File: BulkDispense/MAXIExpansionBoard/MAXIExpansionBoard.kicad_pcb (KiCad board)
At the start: 2 copper layers, 139.7 x 100 mm, 39 parts, among them J1 R0~R5, J10 FS2~FS4, J11 MV1~4, J12 WB/WL, J13 PS/PCV, J14 RV1&2, J15 RV3&4, J16 FS1, J17 FS3, J18 WB-MV1~4, J19 FS2, J2 BS1~4, J20 FS4, J21 BS1~4, J22 OS1~4, J23 WB-MV5~6, J24 LDS, J3 Screw_Terminal_01x02, J4 DigitalOUT 0~3, J5 DigitalOUT 4~7, J6 OS1~4, J7 AnalogIOs, J8 Fan PWR, J9 FS1

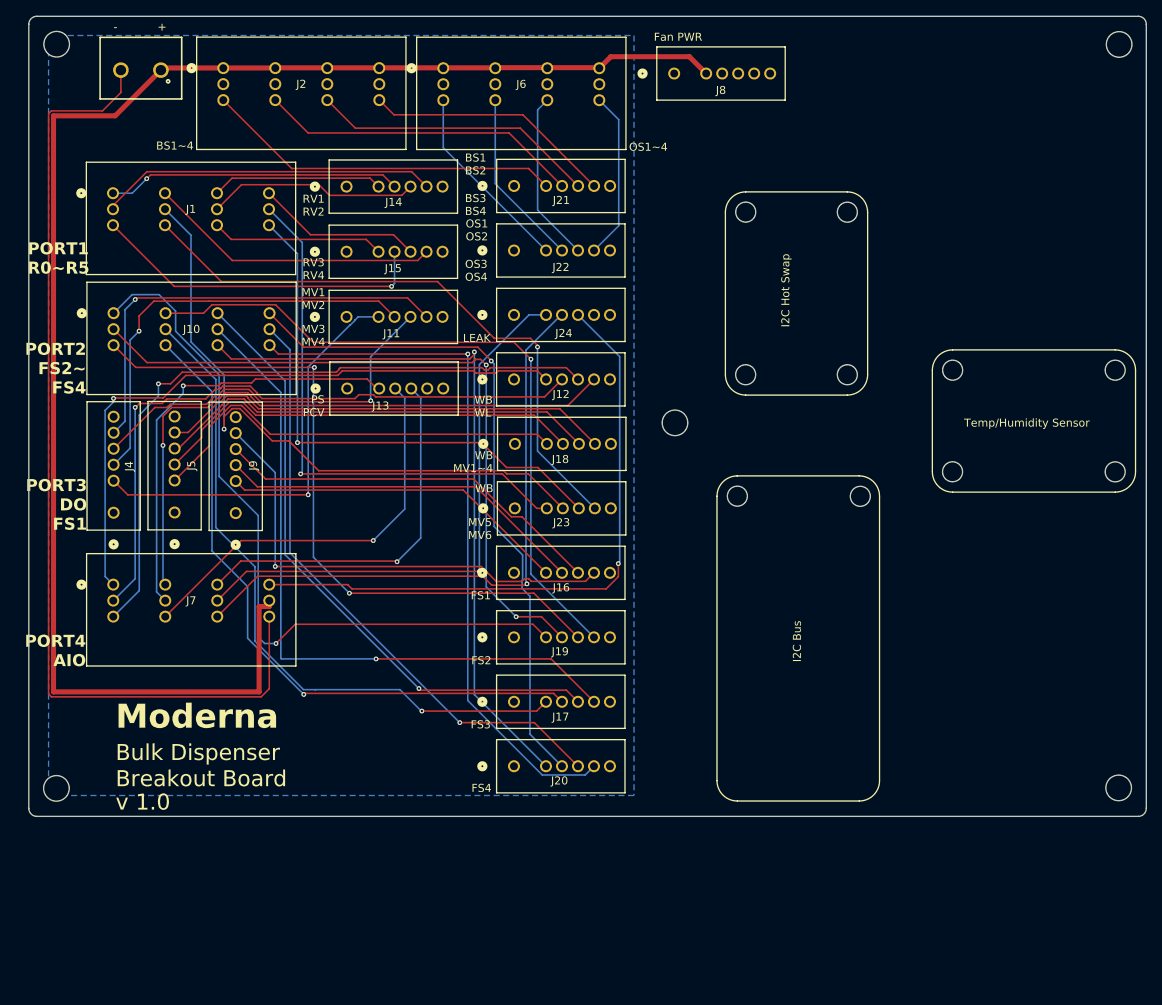
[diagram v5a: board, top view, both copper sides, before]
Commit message: Add PCB Revisions
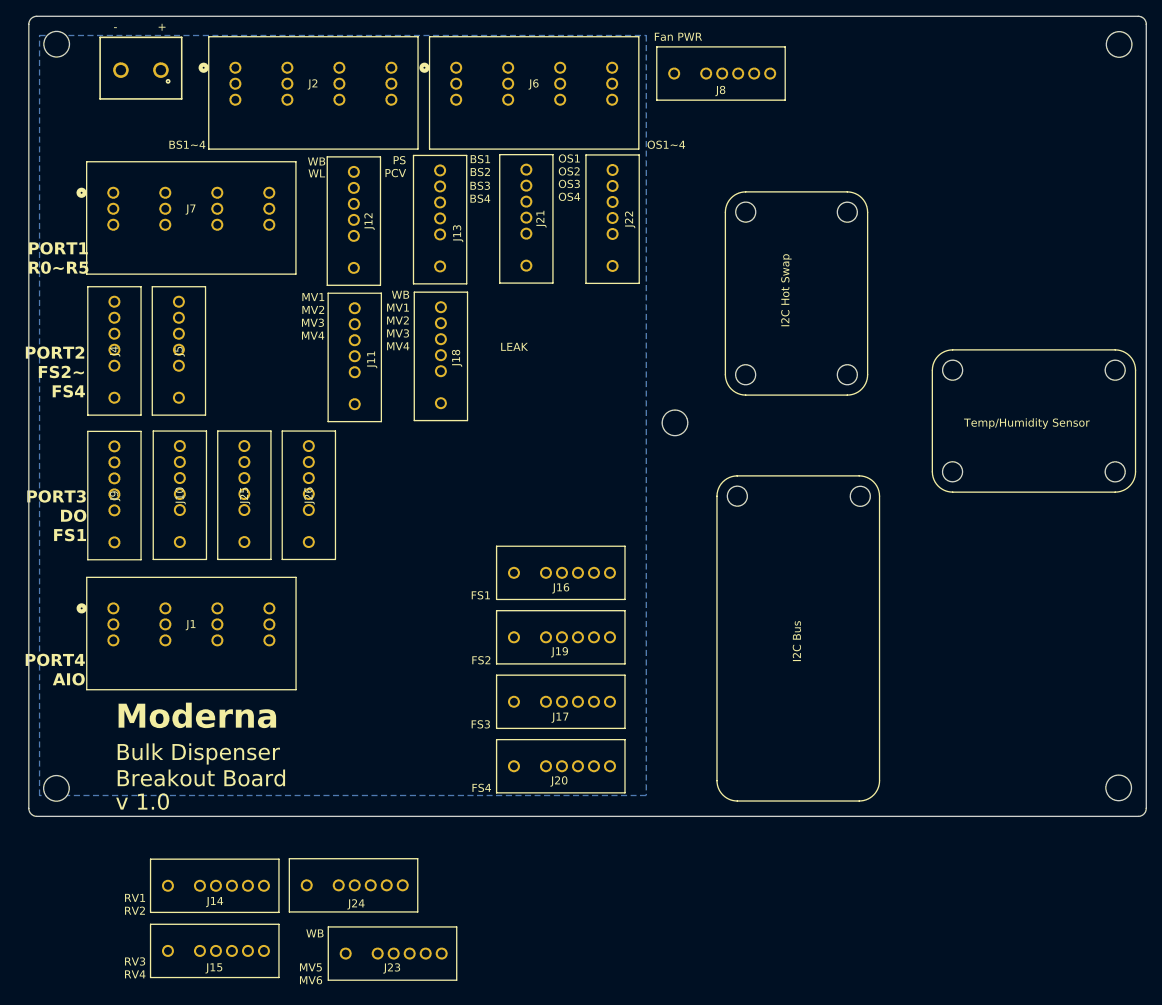
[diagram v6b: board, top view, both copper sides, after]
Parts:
- added J25: FS3, PartsLibrary:CONN_37204-62A3-004PL_3MM, F.Cu at (149.7, 102.1)
- added J26: FS4, PartsLibrary:CONN_37204-62A3-004PL_3MM, F.Cu at (157.8, 102.1)
- J1: value R0~R5 -> PWR
- J10: value FS2~FS4 -> FS2; footprint PartsLibrary:CONN_37212-62M3-003PL_3MM -> PartsLibrary:CONN_37204-62A3-004PL_3MM
- moved J15 90.2 mm to (144.2, 157.2)
- moved J14 90.2 mm to (144.2, 149.0)
- moved J24 75.9 mm to (161.5, 149.0)
- moved J23 59.5 mm to (166.4, 157.5)
- moved J1 51.9 mm to (133.3, 114.4)
- moved J7 49.0 mm to (133.3, 62.4)
- moved J12 30.0 mm to (163.4, 67.8), turned to 90 degrees
- moved J10 26.0 mm to (141.7, 102.1), turned to 90 degrees
- moved J13 20.7 mm to (174.2, 67.6), turned to 90 degrees
- moved J18 16.1 mm to (174.3, 84.7), turned to 90 degrees
- moved J9 15.6 mm to (133.5, 102.1)
- moved J4 14.4 mm to (133.5, 84.0)
- moved J5 14.4 mm to (141.5, 84.0)
- moved J22 8.57 mm to (195.8, 67.6), turned to 90 degrees
- moved J11 7.53 mm to (163.5, 84.8), turned to 90 degrees
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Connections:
- J1 pad 1: /R0_IN -> +24V
- J1 pad 10: /R3_OUT -> /LDS-5V
- J1 pad 11: /R4_OUT -> /LDS
- J1 pad 12: /R5_OUT -> /LDS-GND
- J1 pad 2: /R1_IN -> GND
- J1 pad 3: /R2_IN -> /R0_OUT
- J1 pad 4: /R3_IN -> /R1_OUT
- J1 pad 5: /R4_IN -> /R2_OUT
- J1 pad 6: /R5_IN -> /R3_OUT
- J1 pad 7: /R0_OUT -> /R4_OUT
- J1 pad 8: /R1_OUT -> /R5_OUT
- J1 pad 9: /R2_OUT -> unconnected-(J1-Pin_9-Pad9)
- J10 pad 5: /FS3-1 -> (no net)
- J10 pad 6: /FS3-2 -> (no net)
- J14 pad 2: /R0_IN -> +24V
- J14 pad 4: /R1_IN -> +24V
- J15 pad 2: /R2_IN -> +24V
- J15 pad 4: /R3_IN -> +24V
- J23 pad 2: /R4_IN -> +24V
- J23 pad 4: /R5_IN -> +24V
- J7 pad 10: /LDS -> /AO0
- J7 pad 11: +24V -> unconnected-(J7-Pin_11-Pad11)
- J7 pad 12: GND -> unconnected-(J7-Pin_12-Pad12)
- J7 pad 2: /AI5 -> unconnected-(J7-Pin_2-Pad2)
- J7 pad 3: /AI6 -> /AI5
- J7 pad 4: /AI7 -> /AI6
- J7 pad 5: /AI12 -> unconnected-(J7-Pin_5-Pad5)
- J7 pad 6: /AI13 -> /AI7
- J7 pad 7: /AO0 -> /AI12
- J7 pad 8: /LDS-5V -> unconnected-(J7-Pin_8-Pad8)
- J7 pad 9: /LDS-GND -> /AI13
- J8 pad 2: unconnected-(J8-Pin_2-Pad2) -> GND
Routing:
- net +24V: track 196.9 -> 0.00 mm
- net GND: track 122.6 -> 0.00 mm
- net /FS2-1: track 92.6 -> 0.00 mm, vias 1 -> 0
- net /FS4-1: track 88.9 -> 0.00 mm, vias 1 -> 0
- net /FS2-2: track 88.8 -> 0.00 mm, vias 2 -> 0
- net /FS4-4: track 88.6 -> 0.00 mm, vias 1 -> 0
- net /FS2-3: track 87.2 -> 0.00 mm, vias 2 -> 0
- net /FS2-4: track 87.0 -> 0.00 mm, vias 1 -> 0
- net /FS3-4: track 85.8 -> 0.00 mm, vias 1 -> 0
- net /AI6: track 85.6 -> 0.00 mm, vias 1 -> 0
- net /FS4-2: track 84.6 -> 0.00 mm, vias 1 -> 0
- net /FS3-1: track 84.1 -> 0.00 mm, vias 1 -> 0
- net /FS3-2: track 83.6 -> 0.00 mm, vias 1 -> 0
- net /AI5: track 82.1 -> 0.00 mm, vias 1 -> 0
- net /AI4: track 80.3 -> 0.00 mm, vias 1 -> 0
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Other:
- board text added: "WB MV1 MV2 MV3 MV4"
- board text added: "WL"
- board text removed: "WB MV1~4"
- board text removed: "WB WL"

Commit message: Final Design Changes for Both Boards
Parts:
- removed the J1 at (133.3, 114.4)
- removed J20, J26: FS4, PartsLibrary:CONN_37204-62A3-004PL_3MM
- removed J21: BS1~4, PartsLibrary:CONN_37204-62A3-004PL_3MM
- removed J22: OS1~4, PartsLibrary:CONN_37204-62A3-004PL_3MM
- removed J23: WB-MV5~6, PartsLibrary:CONN_37204-62A3-004PL_3MM
- removed J24: LDS, PartsLibrary:CONN_37204-62A3-004PL_3MM
- removed J25: FS3, PartsLibrary:CONN_37204-62A3-004PL_3MM
- added G***: LOGO, LOGO, F.Cu at (162.4, 64.1)
- added J3: BS1~4, PartsLibrary:CONN_37204-62A3-004PL_3MM, F.Cu at (188.3, 69.5)
- J10: value FS2 -> Signal; footprint PartsLibrary:CONN_37204-62A3-004PL_3MM -> PartsLibrary:CONN26_D13-ST-BK_SUL
- J11: value MV1~4 -> Fan; footprint PartsLibrary:CONN_37204-62A3-004PL_3MM -> PartsLibrary:CONN_37203-62A3-003PL_3MM
- J12: value WB/WL -> Fan; footprint PartsLibrary:CONN_37204-62A3-004PL_3MM -> PartsLibrary:CONN_37203-62A3-003PL_3MM
- J13: value PS/PCV -> WB-MV5; footprint PartsLibrary:CONN_37204-62A3-004PL_3MM -> PartsLibrary:CONN_37203-62A3-003PL_3MM
- J14: value RV1&2 -> WB/WL
- J15: value RV3&4 -> WB-MV1~4
- J16: value FS1 -> WB-MV6; footprint PartsLibrary:CONN_37204-62A3-004PL_3MM -> PartsLibrary:CONN_37203-62A3-003PL_3MM
- J17: value FS3 -> Fan PWR; footprint PartsLibrary:CONN_37204-62A3-004PL_3MM -> PartsLibrary:CONN_37203-62A3-003PL_3MM
- J18: value WB-MV1~4 -> BS1~4; footprint PartsLibrary:CONN_37204-62A3-004PL_3MM -> PartsLibrary:CONN_37212-62M3-003PL_3MM
- J19: value FS2 -> OS1~4; footprint PartsLibrary:CONN_37204-62A3-004PL_3MM -> PartsLibrary:CONN_37212-62M3-003PL_3MM
- J2: value BS1~4 -> MV1~4; footprint PartsLibrary:CONN_37212-62M3-003PL_3MM -> PartsLibrary:CONN_37204-62A3-004PL_3MM
- J4: value DigitalOUT 0~3 -> I2C; footprint PartsLibrary:CONN_37204-62A3-004PL_3MM -> PartsLibrary:CONN_37203-62A3-003PL_3MM
- J5: value DigitalOUT 4~7 -> PS/PCV/LDS
- J6: footprint PartsLibrary:CONN_37212-62M3-003PL_3MM -> PartsLibrary:CONN_37204-62A3-004PL_3MM
- J7: value AnalogIOs -> Fan; footprint PartsLibrary:CONN_37212-62M3-003PL_3MM -> PartsLibrary:CONN_37203-62A3-003PL_3MM
- J8: value Fan PWR -> RV1; footprint PartsLibrary:CONN_37204-62A3-004PL_3MM -> PartsLibrary:CONN_37203-62A3-003PL_3MM
- J9: value FS1 -> Fan; footprint PartsLibrary:CONN_37204-62A3-004PL_3MM -> PartsLibrary:CONN_37203-62A3-003PL_3MM
- moved J17 86.5 mm to (214.1, 43.8)
- moved J14 81.1 mm to (196.0, 86.7), turned to 90 degrees
- moved J19 74.1 mm to (177.1, 44.6)
- moved J15 73.5 mm to (165.6, 86.8), turned to 90 degrees
- moved J8 73.3 mm to (158.3, 101.8), turned to 90 degrees
- moved J7 60.5 mm to (188.6, 86.9), turned to 90 degrees
- moved J2 51.4 mm to (180.7, 86.9), turned to 90 degrees
- moved H6 47.6 mm to (258.5, 53.0), turned to -90 degrees
- moved J18 47.1 mm to (149.6, 44.6), turned to 0 degrees
- moved H8 41.2 mm to (238.2, 53.0), turned to -90 degrees
- moved J12 38.3 mm to (181.1, 101.8)
- moved J13 37.2 mm to (188.7, 101.8)
- moved H7 33.9 mm to (212.5, 66.4)
- moved H9 33.9 mm to (227.9, 66.5)
- moved H7 33.4 mm to (258.5, 65.7), turned to -90 degrees
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- renumbered H9 to H10, H10 to H11, H11 to H2, H2 to H3, H3 to H4, H4 to H5, H5 to H6, H6 to H7, H6 to H8, H9 to H8, H10 to H9, H8 to H9, J3 to J1
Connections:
- J10 pad 1: /FS2-1 -> +24V
- J10 pad 2: /FS2-2 -> GND
- J10 pad 3: /FS2-3 -> /SDA
- J10 pad 4: /FS2-4 -> /SCL
- J10 pad 5: (no net) -> /LDS
- J10 pad 6: (no net) -> /AI4
- J11 pad 1: /DO0 -> +24V
- J11 pad 2: /DO1 -> unconnected-(J11-Pin_2-Pad2)
- J11 pad 3: /DO2 -> /R2_OUT
- J12 pad 1: /AI4 -> +24V
- J12 pad 2: /AI5 -> unconnected-(J12-Pin_2-Pad2)
- J12 pad 3: /AI6 -> /R3_OUT
- J13 pad 1: /AI12 -> +24V
- J13 pad 2: /AI13 -> unconnected-(J13-Pin_2-Pad2)
- J13 pad 3: /AO0 -> /R4_OUT
- J14 pad 1: /R0_OUT -> /AI4
- J14 pad 2: +24V -> /AI5
- J14 pad 3: /R1_OUT -> /AI6
- J14 pad 4: +24V -> /AI7
- J15 pad 1: /R2_OUT -> /DO4
- J15 pad 2: +24V -> /DO5
- J15 pad 3: /R3_OUT -> /DO6
- J15 pad 4: +24V -> /DO7
- J16 pad 1: /FS1-1 -> +24V
- J16 pad 2: /FS1-2 -> unconnected-(J16-Pin_2-Pad2)
- J16 pad 3: /FS1-3 -> /R5_OUT
- J17 pad 1: /FS3-1 -> /R6_OUT
- J17 pad 2: /FS3-2 -> unconnected-(J17-Pin_2-Pad2)
- J17 pad 3: /FS3-3 -> GND
- J18 pad 1: /DO4 -> +24V
- J18 pad 2: /DO5 -> GND
- J18 pad 3: /DO6 -> /AI0
- J18 pad 4: /DO7 -> +24V
- J18 pad 5: (no net) -> GND
- J18 pad 6: (no net) -> /AI1
- J19 pad 1: /FS2-1 -> +24V
- J19 pad 2: /FS2-2 -> GND
- J19 pad 3: /FS2-3 -> /DI0
- J19 pad 4: /FS2-4 -> +24V
- J19 pad 5: (no net) -> GND
- J19 pad 6: (no net) -> /DI1
- J2 pad 1: +24V -> /DO0
- J2 pad 2: GND -> /DO1
- J2 pad 3: /AI0 -> /DO2
- J2 pad 4: +24V -> /DO3
- J2 pad 5: GND -> (no net)
- J2 pad 6: /AI1 -> (no net)
- J4 pad 1: /DO0 -> /SCL
- J4 pad 2: /DO1 -> unconnected-(J4-Pin_2-Pad2)
- J4 pad 3: /DO2 -> /SDA
- J5 pad 1: /DO4 -> /AI12
- J5 pad 2: /DO5 -> /AI13
- J5 pad 3: /DO6 -> /AO0
- J5 pad 4: /DO7 -> /LDS
- J6 pad 1: +24V -> /DI0
- J6 pad 2: GND -> /DI1
- J6 pad 3: /DI0 -> /DI2
- J6 pad 4: +24V -> /DI3
- J6 pad 5: GND -> (no net)
- J6 pad 6: /DI1 -> (no net)
- J7 pad 1: /AI4 -> +24V
- J7 pad 3: /AI5 -> /R6_OUT
- J8 pad 2: GND -> unconnected-(J8-Pin_2-Pad2)
- J8 pad 3: /R6_OUT -> /R0_OUT
- J9 pad 1: /FS1-1 -> +24V
- J9 pad 2: /FS1-2 -> unconnected-(J9-Pin_2-Pad2)
- J9 pad 3: /FS1-3 -> /R1_OUT
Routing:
- net +24V: track 0.00 -> 239.2 mm
- net /R5_OUT: track 0.00 -> 77.4 mm, vias 0 -> 1
- net /AI6: track 0.00 -> 75.5 mm
- net /AI5: track 0.00 -> 73.5 mm
- net /AI7: track 0.00 -> 72.3 mm
- net /R4_OUT: track 0.00 -> 72.3 mm, vias 0 -> 1
- net /AI4: track 0.00 -> 72.0 mm, vias 0 -> 1
- net /R2_OUT: track 0.00 -> 61.9 mm, vias 0 -> 1
- net /LDS: track 0.00 -> 61.1 mm, vias 0 -> 1
- net /R3_OUT: track 0.00 -> 61.0 mm, vias 0 -> 1
- net /DO0: track 0.00 -> 58.4 mm
- net /DO2: track 0.00 -> 55.7 mm
- net /DO1: track 0.00 -> 53.6 mm
- net /DO3: track 0.00 -> 52.3 mm
- net /AI13: track 0.00 -> 52.0 mm
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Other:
- board size 139.7 x 100 mm -> 139.7 x 75.2 mm
- board text added: "BS"
- board text added: "BS1"
- board text added: "BS2"
- board text added: "BS3"
- board text added: "BS4"
- board text added: "Electrical"
- board text added: "Fan"
- board text added: "I2C"
- board text added: "MV1~4"
- board text added: "OS"
- board text added: "OS1"
- board text added: "OS2"
- board text added: "OS3"
- board text added: "OS4"
- board text added: "PS/PCV/LDS"
- board text added: "RV1"
- board text added: "RV2"
- board text added: "RV3"
- board text added: "RV4"
- board text added: "Temperature Humidity Sensor"
- board text added: "WB-MV1~4"
- board text added: "WB-MV5"
- board text added: "WB-MV6"
- board text added: "WB/WL"
- board text added: "v 2.0"
- board text removed: "BS1 BS2"
- board text removed: "BS1~4"
- board text removed: "BS3 BS4"
- board text removed: "FS1"
- board text removed: "FS2"
- board text removed: "FS3"
- board text removed: "FS4"
- board text removed: "LEAK"
- board text removed: "MV1 MV2"
- board text removed: "MV3 MV4"
- board text removed: "MV5 MV6"
- board text removed: "Moderna"
- board text removed: "OS1 OS2"
- board text removed: "OS1~4"
- board text removed: "OS3 OS4"
- board text removed: "PORT1 R0~R5"
- board text removed: "PORT2 FS2~ FS4"
- board text removed: "PORT3 DO FS1"
- board text removed: "PORT4 AIO"
- board text removed: "PS PCV"
- board text removed: "RV1 RV2"
- board text removed: "RV3 RV4"
- board text removed: "Temp/Humidity Sensor"
- board text removed: "WB"
- board text removed: "WB MV1 MV2 MV3 MV4"
- board text removed: "WL"
- board text removed: "v 1.0"
